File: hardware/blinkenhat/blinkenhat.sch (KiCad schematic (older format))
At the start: 26 parts, among them J1 LED1, J2 LED2, J3 INPUT, J4 Programmer, J5 USB_POWER, J6 GPIO, Q1 2N7002, Q2 2N7002, SW1 RESET, U1 AMS1117-3V3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

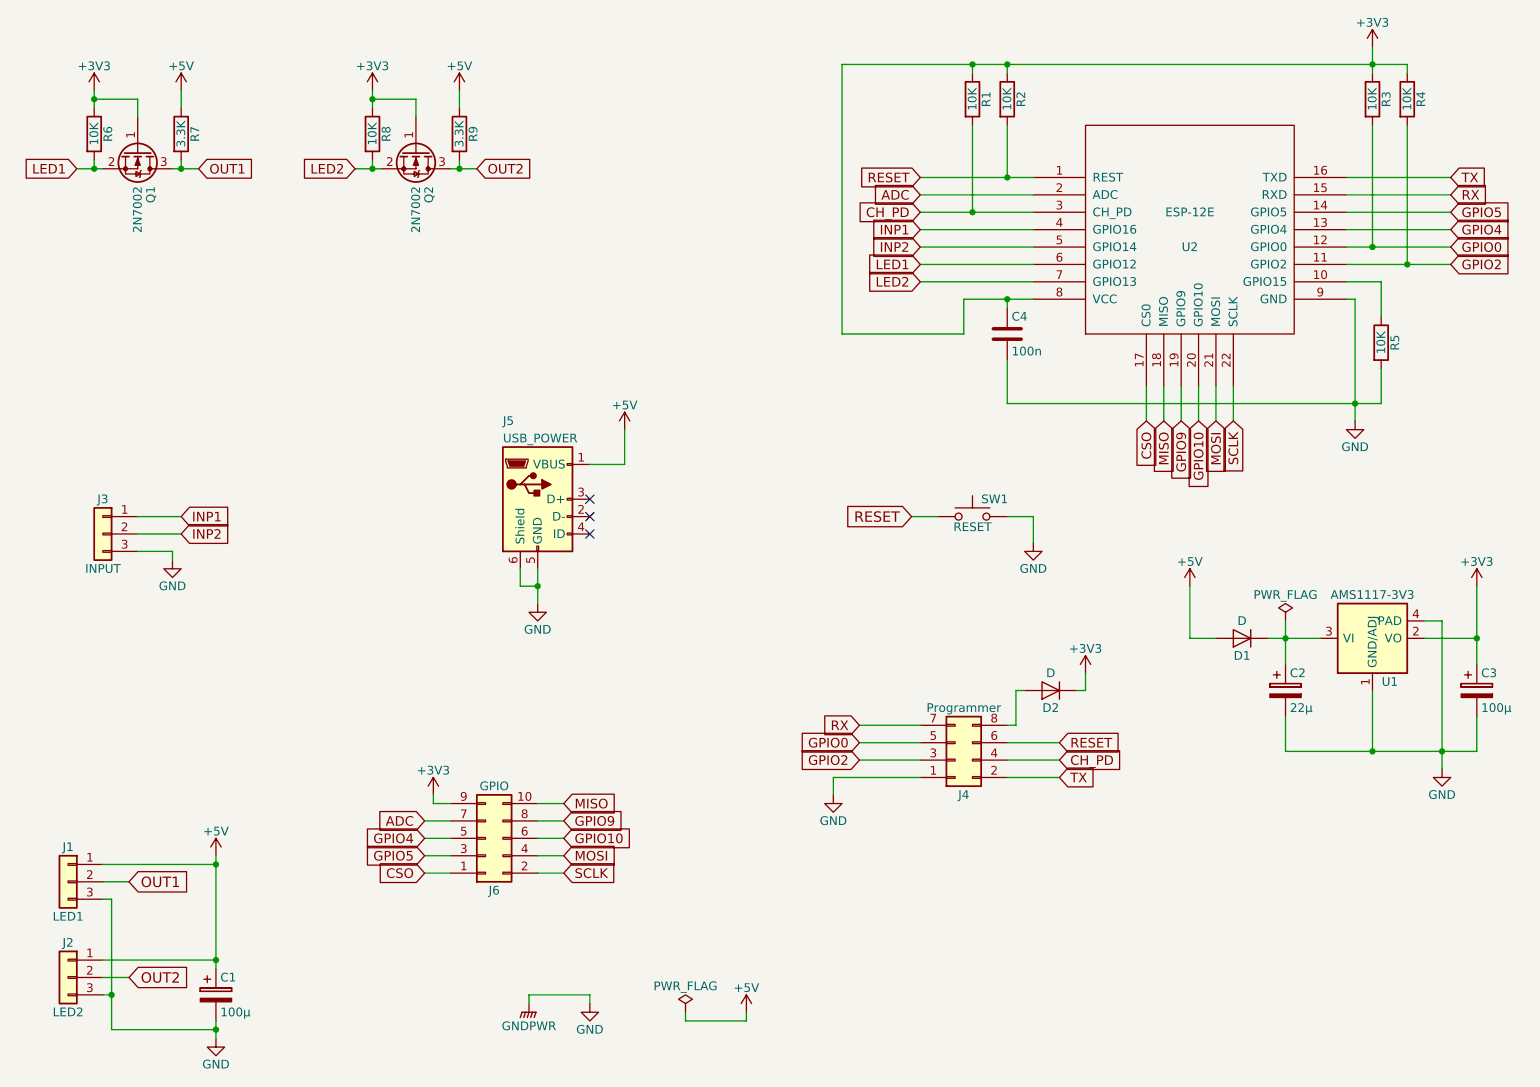
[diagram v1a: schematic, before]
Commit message: Hardware: change capacitors vor 3V3.
Signed-off-by: Jan Losinski <losinski@wh2.tu-dresden.de>
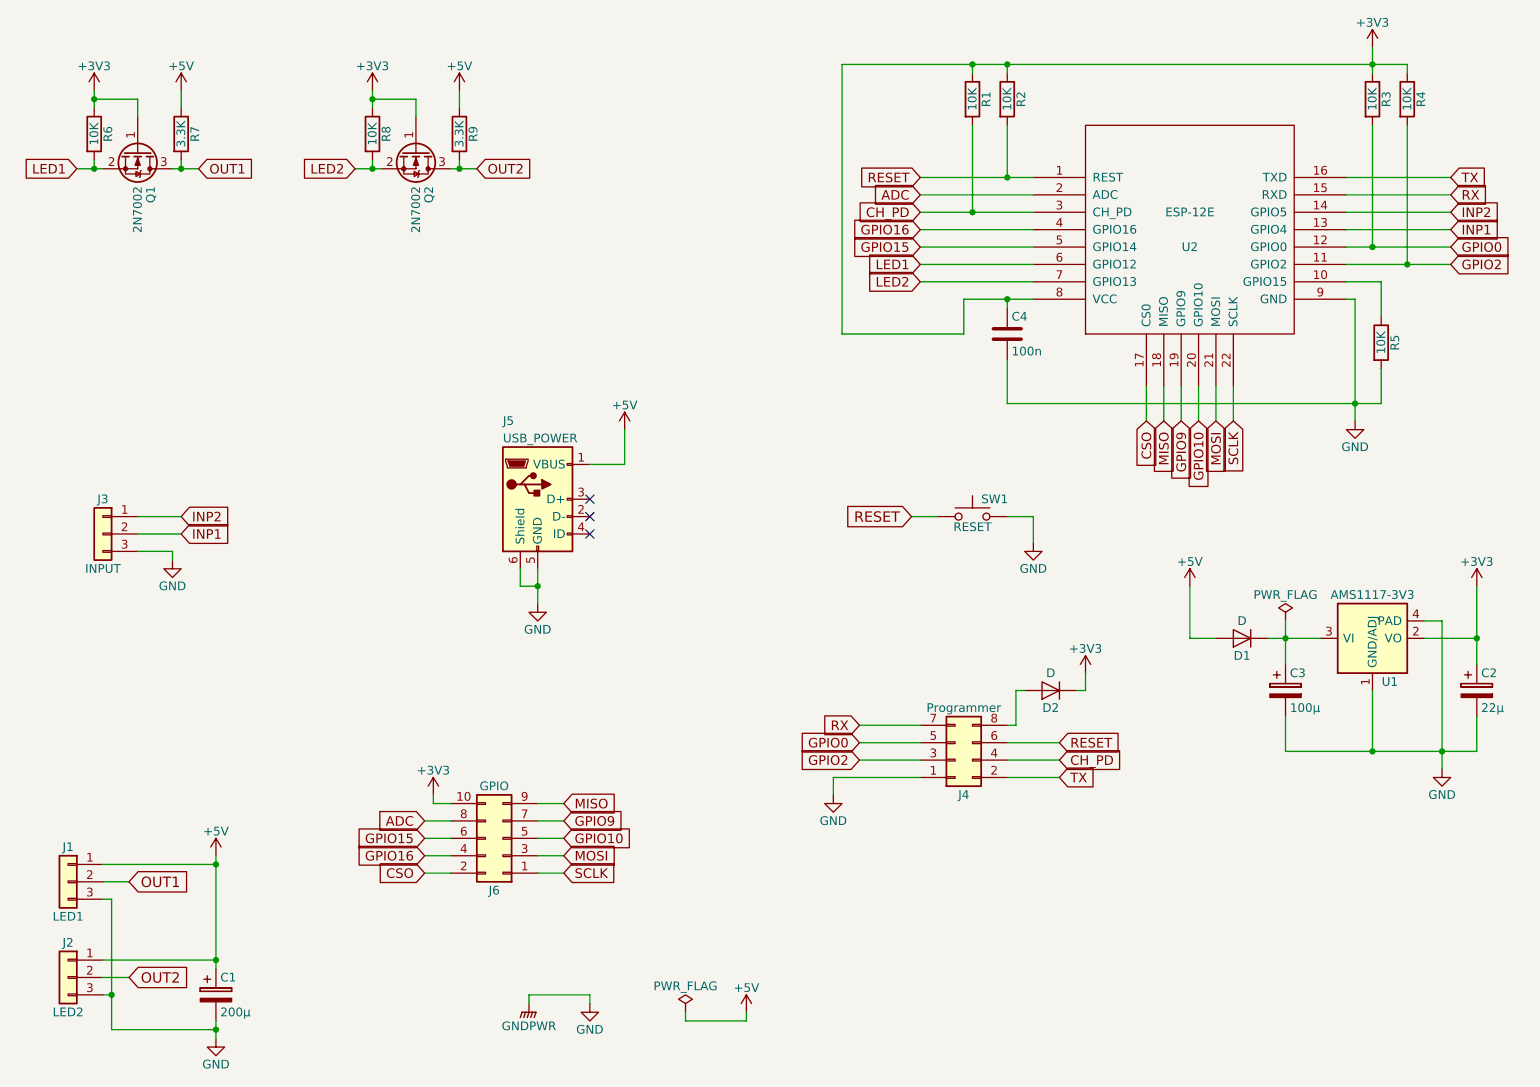
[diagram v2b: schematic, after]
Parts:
- C1: value 100µ -> 200µ; footprint Capacitors_SMD:CP_Elec_6.3x5.8 -> Capacitors_Tantalum_SMD:CP_Tantalum_Case-C_EIA-6032-28_Reflow
- C2: renamed from C3; value 100µ -> 22µ; footprint Capacitors_SMD:CP_Elec_6.3x5.8 -> Capacitors_Tantalum_SMD:CP_Tantalum_Case-B_EIA-3528-21_Reflow
- C3: renamed from C2; value 22µ -> 100µ; footprint Capacitors_SMD:CP_Elec_5x5.3 -> Capacitors_Tantalum_SMD:CP_Tantalum_Case-C_EIA-6032-28_Reflow
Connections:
- net +3V3: now also J6.10 (Pin_10); no longer J6.9 (Pin_9)
- net ADC: now also J6.8 (Pin_8); no longer J6.7 (Pin_7)
- net CSO: now also J6.2 (Pin_2); no longer J6.1 (Pin_1)
- net GPIO10: now also J6.5 (Pin_5); no longer J6.6 (Pin_6)
- net GPIO9: now also J6.7 (Pin_7); no longer J6.8 (Pin_8)
- net INP1: now also J3.2 (Pin_2), U2.13 (GPIO4); no longer J3.1 (Pin_1), U2.4 (GPIO16)
- net INP2: now also J3.1 (Pin_1), U2.14 (GPIO5); no longer J3.2 (Pin_2), U2.5 (GPIO14)
- net MISO: now also J6.9 (Pin_9); no longer J6.10 (Pin_10)
- net MOSI: now also J6.3 (Pin_3); no longer J6.4 (Pin_4)
- net SCLK: now also J6.1 (Pin_1); no longer J6.2 (Pin_2)
- removed net GPIO4: J6.5 (Pin_5), U2.13 (GPIO4)
- removed net GPIO5: J6.3 (Pin_3), U2.14 (GPIO5)
- new net GPIO15: J6.6 (Pin_6), U2.5 (GPIO14)
- new net GPIO16: J6.4 (Pin_4), U2.4 (GPIO16)
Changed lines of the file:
@@
 Title "BlinkenHat"
 Date "2018-01-04"
-Rev "0.1"
+Rev "0.2"
 Comp "Retardigrades"
 Comment1 ""
@@
 $EndComp
 $Comp
-L CP C2
+L CP C3
 U 1 1 5A4D735C
 P 8800 5150
-F 0 "C2" H 8825 5250 50  0000 L CNN
-F 1 "22µ" H 8825 5050 50  0000 L CNN
-F 2 "Capacitors_SMD:CP_Elec_5x5.3" H 8838 5000 50  0001 C CNN
+F 0 "C3" H 8825 5250 50  0000 L CNN
+F 1 "100µ" H 8825 5050 50  0000 L CNN
+F 2 "Capacitors_Tantalum_SMD:CP_Tantalum_Case-C_EIA-6032-28_Reflow" H 8838 5000 50  0001 C CNN
 F 3 "" H 8800 5150 50  0001 C CNN
 	1    8800 5150
@@
 $EndComp
 $Comp
-L CP C3
+L CP C2
 U 1 1 5A4D74E9
 P 9900 5150
-F 0 "C3" H 9925 5250 50  0000 L CNN
-F 1 "100µ" H 9925 5050 50  0000 L CNN
-F 2 "Capacitors_SMD:CP_Elec_6.3x5.8" H 9938 5000 50  0001 C CNN
+F 0 "C2" H 9925 5250 50  0000 L CNN
+F 1 "22µ" H 9925 5050 50  0000 L CNN
+F 2 "Capacitors_Tantalum_SMD:CP_Tantalum_Case-B_EIA-3528-21_Reflow" H 9938 5000 50  0001 C CNN
 F 3 "" H 9900 5150 50  0001 C CNN
 	1    9900 5150
@@
 LED2
 Text GLabel 6700 2500 0    55   Input ~ 0
-INP1
+GPIO16
 Text GLabel 6700 2600 0    55   Input ~ 0
-INP2
+GPIO15
 $Comp
 L +3V3 #PWR09
@@
 P 2650 6900
 F 0 "C1" H 2675 7000 50  0000 L CNN
-F 1 "100µ" H 2675 6800 50  0000 L CNN
-F 2 "Capacitors_SMD:CP_Elec_6.3x5.8" H 2688 6750 50  0001 C CNN
+F 1 "200µ" H 2675 6800 50  0000 L CNN
+F 2 "Capacitors_Tantalum_SMD:CP_Tantalum_Case-C_EIA-6032-28_Reflow" H 2688 6750 50  0001 C CNN
 F 3 "" H 2650 6900 50  0001 C CNN
 	1    2650 6900
@@
 $EndComp
 Text GLabel 2450 4250 2    55   Input ~ 0
+INP1
+Text GLabel 2450 4150 2    55   Input ~ 0
 INP2
-Text GLabel 2450 4150 2    55   Input ~ 0
-INP1
 $Comp
 L GND #PWR013
@@
 L Conn_02x05_Odd_Even J6
 U 1 1 5A4EBCE1
-P 4200 6000
-F 0 "J6" H 4250 6300 50  0000 C CNN
-F 1 "GPIO" H 4250 5700 50  0000 C CNN
-F 2 "Pin_Headers:Pin_Header_Straight_2x05_Pitch1.27mm" H 4200 6000 50  0001 C CNN
-F 3 "" H 4200 6000 50  0001 C CNN
-	1    4200 6000
-	1    0    0    1
+P 4300 6000
+F 0 "J6" H 4350 6300 50  0000 C CNN
+F 1 "GPIO" H 4350 5700 50  0000 C CNN
+F 2 "Pin_Headers:Pin_Header_Straight_2x05_Pitch1.27mm" H 4300 6000 50  0001 C CNN
+F 3 "" H 4300 6000 50  0001 C CNN
+	1    4300 6000
+	-1   0    0    1
 $EndComp
 Text GLabel 6700 2300 0    55   Input ~ 0
 ADC
 Text GLabel 9750 2400 2    55   Input ~ 0
-GPIO5
+INP2
 Text GLabel 9750 2500 2    55   Input ~ 0
-GPIO4
+INP1
 Text GLabel 8200 3600 3    55   Input ~ 0
 GPIO9
@@
 ADC
 Text GLabel 3850 6100 0    55   Input ~ 0
-GPIO5
+GPIO16
 Text GLabel 3850 6000 0    55   Input ~ 0
-GPIO4
+GPIO15
 Text GLabel 3850 6200 0    55   Input ~ 0
 CSO
@@
 	9300 5150 9300 5500
 Wire Wire Line
-	9900 4550 9900 4850
-Wire Wire Line
-	9900 4850 9900 5000
+	9900 4550 9900 5000
 Wire Wire Line
 	9900 4850 9600 4850
@@
 	9600 4750 9700 4750
 Wire Wire Line
-	9700 4750 9700 5500
-Wire Wire Line
-	9700 5500 9700 5600
+	9700 4750 9700 5600
 Connection ~ 9300 5500
 Wire Wire Line
 	8800 5300 8800 5500
 Wire Wire Line
-	8800 5500 9300 5500
-Wire Wire Line
-	9300 5500 9700 5500
-Wire Wire Line
-	9700 5500 9900 5500
+	8800 5500 9900 5500
 Connection ~ 8800 4850
 Wire Wire Line
@@
 Connection ~ 9900 4850
 Wire Wire Line
-	4500 4450 4500 4550
-Wire Wire Line
-	4500 4550 4500 4650
+	4500 4450 4500 4650
 Wire Wire Line
 	4500 4550 4400 4550
@@
 	7250 5350 7200 5350
 Wire Wire Line
-	9150 2600 9300 2600
-Wire Wire Line
-	9300 2600 9750 2600
+	9150 2600 9750 2600
 Wire Wire Line
 	9300 2600 9300 1900
@@
 	9500 1900 9500 2700
 Wire Wire Line
-	9150 2700 9500 2700
-Wire Wire Line
-	9500 2700 9750 2700
+	9150 2700 9750 2700
 Wire Wire Line
 	9150 2800 9350 2800
@@
 	9150 2900 9200 2900
 Wire Wire Line
-	9200 2900 9200 3500
-Wire Wire Line
-	9200 3500 9200 3600
+	9200 2900 9200 3600
 Wire Wire Line
 	9350 3500 9350 3300
@@
 	7200 1900 7200 2200
 Wire Wire Line
-	6700 2200 7200 2200
-Wire Wire Line
-	7200 2200 7350 2200
+	6700 2200 7350 2200
 Wire Wire Line
 	7000 1900 7000 2400
 Wire Wire Line
-	6700 2400 7000 2400
-Wire Wire Line
-	7000 2400 7350 2400
+	6700 2400 7350 2400
 Wire Wire Line
 	7000 1600 7000 1550
 Wire Wire Line
-	6250 1550 7000 1550
-Wire Wire Line
-	7000 1550 7200 1550
-Wire Wire Line
-	7200 1550 9300 1550
-Wire Wire Line
-	9300 1550 9500 1550
+	6250 1550 9500 1550
 Wire Wire Line
 	7200 1550 7200 1600
@@
 	6700 2800 7350 2800
 Wire Wire Line
-	6950 2900 7200 2900
-Wire Wire Line
-	7200 2900 7350 2900
+	6950 2900 7350 2900
 Wire Wire Line
 	6950 2900 6950 3100
@@
 	6250 3100 6250 1550
 Wire Wire Line
-	9300 1450 9300 1550
-Wire Wire Line
-	9300 1550 9300 1600
+	9300 1450 9300 1600
 Connection ~ 7200 1550
 Wire Wire Line
@@
 Connection ~ 9300 1550
 Wire Wire Line
-	7200 3500 9200 3500
-Wire Wire Line
-	9200 3500 9350 3500
+	7200 3500 9350 3500
 Wire Wire Line
 	7200 3500 7200 3250
@@
 	2000 6350 2050 6350
 Wire Wire Line
-	2050 6350 2050 6900
-Wire Wire Line
-	2050 6900 2050 7100
-Wire Wire Line
-	2650 6100 2650 6150
-Wire Wire Line
-	2650 6150 2650 6700
-Wire Wire Line
-	2650 6700 2650 6750
+	2050 6350 2050 7100
+Wire Wire Line
+	2650 6100 2650 6750
 Connection ~ 2650 6700
 Wire Wire Line
 	2050 7100 2650 7100
 Wire Wire Line
-	2650 7050 2650 7100
-Wire Wire Line
-	2650 7100 2650 7150
+	2650 7050 2650 7150
 Connection ~ 2050 6900
 Wire Wire Line
@@
 	3550 2100 3550 2150
 Wire Wire Line
-	3450 2150 3550 2150
-Wire Wire Line
-	3550 2150 3600 2150
-Wire Wire Line
-	4000 2150 4050 2150
-Wire Wire Line
-	4050 2150 4150 2150
+	3450 2150 3600 2150
+Wire Wire Line
+	4000 2150 4150 2150
 Wire Wire Line
 	4050 2150 4050 2100
 Wire Wire Line
-	2400 2150 2450 2150
-Wire Wire Line
-	2450 2150 2550 2150
+	2400 2150 2550 2150
 Wire Wire Line
 	2450 2150 2450 2100
@@
 	1950 2100 1950 2150
 Wire Wire Line
-	1850 2150 1950 2150
-Wire Wire Line
-	1950 2150 2000 2150
+	1850 2150 2000 2150
 Wire Wire Line
 	2200 1850 2200 1750
@@
 	2200 1750 1950 1750
 Wire Wire Line
-	1950 1700 1950 1750
-Wire Wire Line
-	1950 1750 1950 1800
+	1950 1700 1950 1800
 Wire Wire Line
 	3800 1850 3800 1750
@@
 	3800 1750 3550 1750
 Wire Wire Line
-	3550 1700 3550 1750
-Wire Wire Line
-	3550 1750 3550 1800
+	3550 1700 3550 1800
 Wire Wire Line
 	4050 1700 4050 1800
@@
 	5700 7050 5700 7000
 Wire Wire Line
-	8800 4750 8800 4850
-Wire Wire Line
-	8800 4850 8800 5000
-Wire Wire Line
-	8700 4850 8800 4850
-Wire Wire Line
-	8800 4850 9000 4850
+	8800 4750 8800 5000
+Wire Wire Line
+	8700 4850 9000 4850
 Wire Wire Line
 	8400 4850 8250 4850

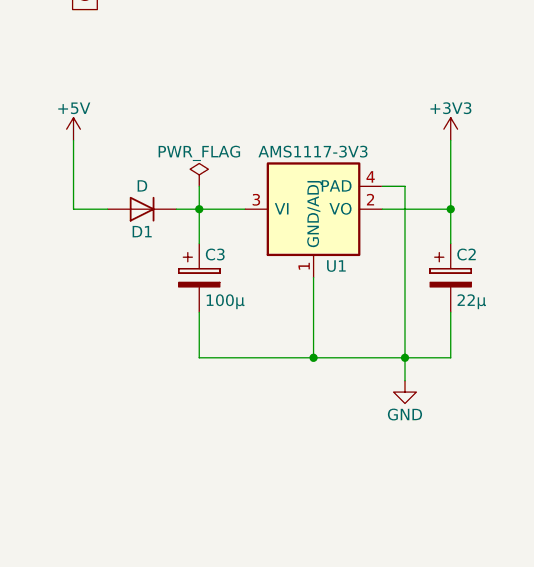
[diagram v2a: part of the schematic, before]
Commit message: Hardware: fix wrong connection of heat pad for AMS
Signed-off-by: Jan Losinski <losinski@wh2.tu-dresden.de>
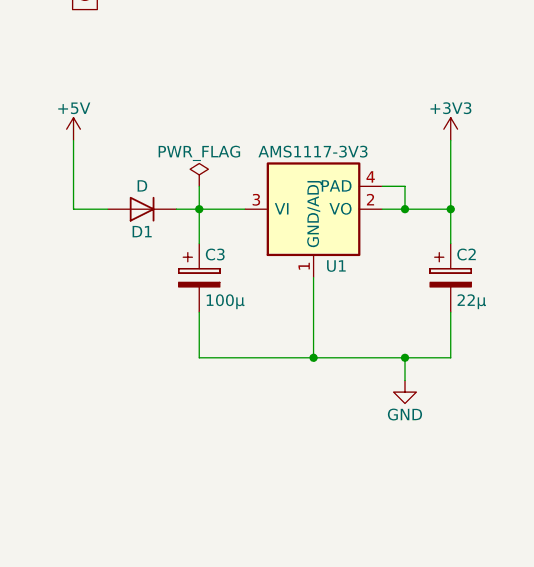
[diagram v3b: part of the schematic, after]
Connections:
- net +3V3: now also U1.4 (PAD)
- net GND: no longer U1.4 (PAD)
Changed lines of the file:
@@
 Wire Wire Line
 	9600 4750 9700 4750
-Wire Wire Line
-	9700 4750 9700 5600
 Connection ~ 9300 5500
 Wire Wire Line
@@
 Wire Wire Line
 	3900 5800 4000 5800
+Wire Wire Line
+	9700 5500 9700 5600
+Wire Wire Line
+	9700 4750 9700 4850
+Connection ~ 9700 4850
 $EndSCHEMATC

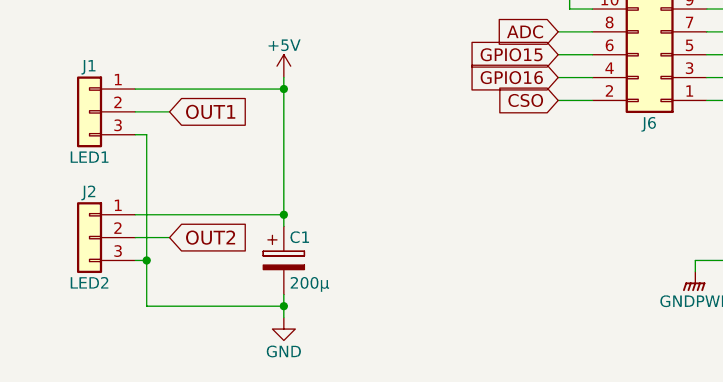
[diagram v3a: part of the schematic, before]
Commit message: Hardware: adjust with reality.
Signed-off-by: Jan Losinski <losinski@wh2.tu-dresden.de>
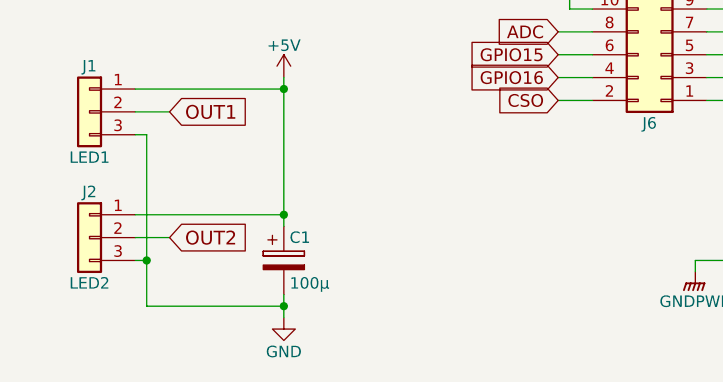
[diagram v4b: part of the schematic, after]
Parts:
- C1: value 200µ -> 100µ
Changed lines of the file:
@@
 P 2650 6900
 F 0 "C1" H 2675 7000 50  0000 L CNN
-F 1 "200µ" H 2675 6800 50  0000 L CNN
+F 1 "100µ" H 2675 6800 50  0000 L CNN
 F 2 "Capacitors_Tantalum_SMD:CP_Tantalum_Case-C_EIA-6032-28_Reflow" H 2688 6750 50  0001 C CNN
 F 3 "" H 2650 6900 50  0001 C CNN
